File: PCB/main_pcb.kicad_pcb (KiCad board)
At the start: 2 copper layers, 116.9 x 116.9 mm, 39 parts, among them P1 SEN, P2 SRV, P3 PWR, P4 LED, P5 M1, P6 M2, P7 CONN_02X03, P8 CONN_02X03, Q1 5LN01SP, U1 Teensy_3.1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

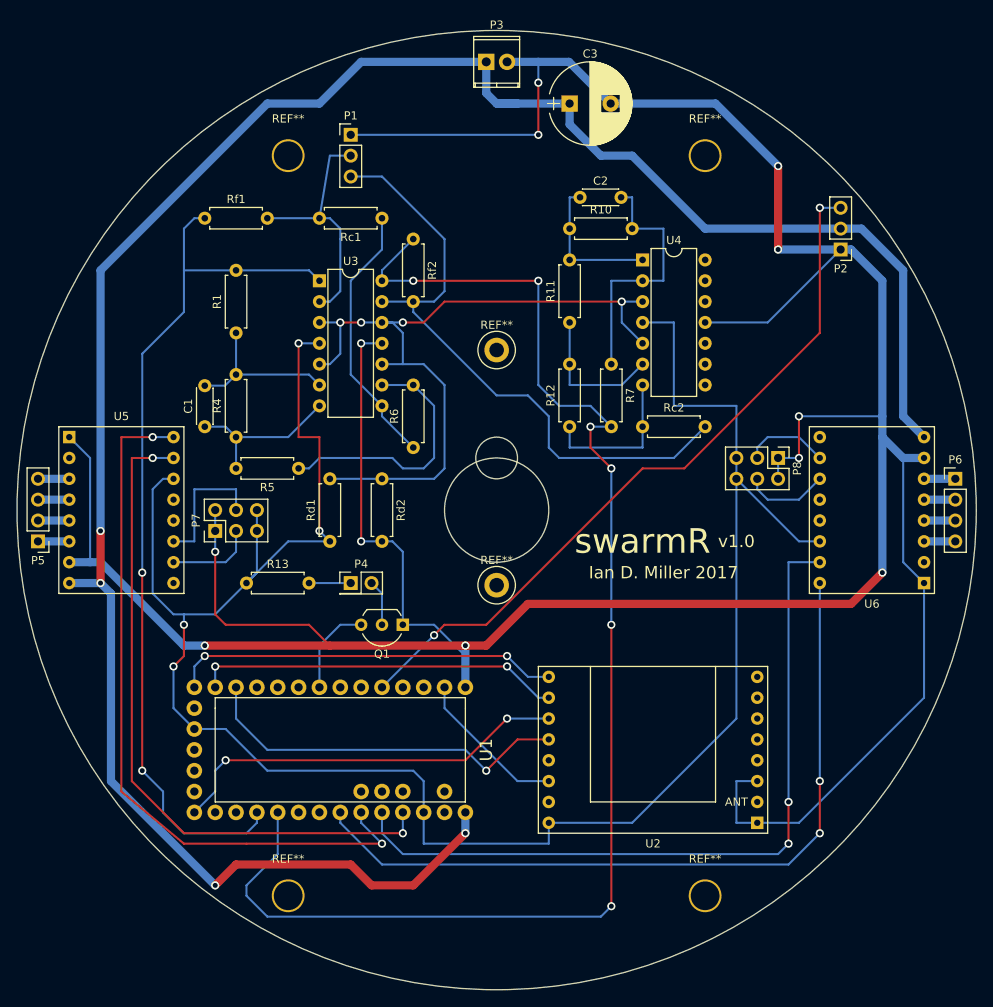
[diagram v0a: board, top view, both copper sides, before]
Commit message: Updated pcb layout for easier fabrication
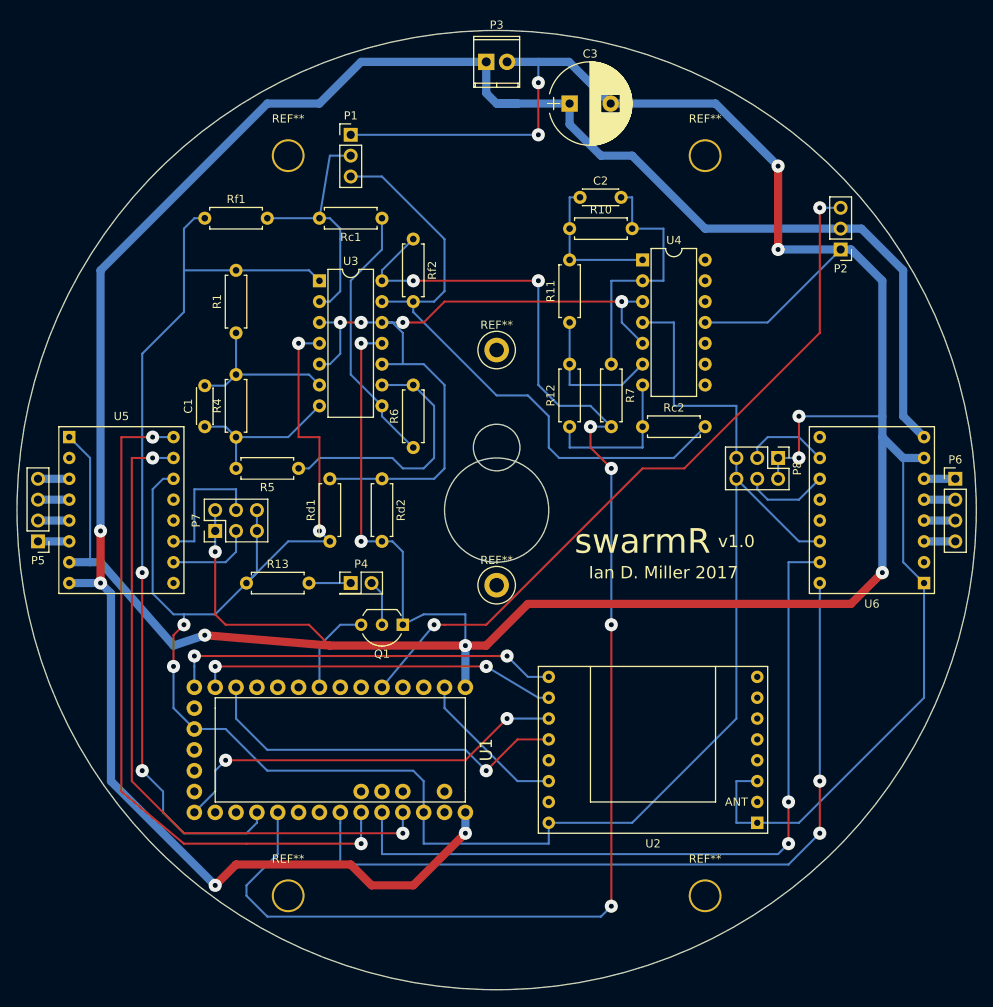
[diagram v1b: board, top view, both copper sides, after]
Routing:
- net GND: track 454.5 -> 458.9 mm
- net /DIR1: track 88.4 -> 84.8 mm
- net /DIR2: track 93.9 -> 96.8 mm
- net /STEP2: track 91.7 -> 93.2 mm
- net /MISO: track 47.3 -> 48.0 mm
- net /MOSI: track 44.8 -> 44.2 mm
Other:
- outline, holes or cut-outs redrawn
- net class Default: via_dia 1 -> 1.6

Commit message: minor pcb and BOM adjustments
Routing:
- net /RadCS: vias 1 -> 2

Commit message: Small pcb adjustments
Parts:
- R13: value R -> 10R
- Rc1, Rc2: value 15k -> 240k
- Rf1, Rf2: value 51k -> 750k
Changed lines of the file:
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@@
     (links 99)
     (no_connects 0)
-    (area 79.921196 35.01412 215.01 165.260001)
+    (area 79.921196 36.741196 196.938804 153.758804)
     (thickness 1.6)
     (drawings 9)
@@
       (padsonsilk false)
       (subtractmaskfromsilk false)
-      (outputformat 1)
+      (outputformat 4)
       (mirror false)
       (drillshape 0)
@@
       (effects (font (size 1 1) (thickness 0.15)))
     )
-    (fp_text value R (at 3.81 2.31) (layer F.Fab)
+    (fp_text value 10R (at 3.81 2.31) (layer F.Fab)
       (effects (font (size 1 1) (thickness 0.15)))
     )
@@
       (effects (font (size 1 1) (thickness 0.15)))
     )
-    (fp_text value 15k (at 3.81 2.31 180) (layer F.Fab)
+    (fp_text value 240k (at 3.81 2.31 180) (layer F.Fab)
       (effects (font (size 1 1) (thickness 0.15)))
     )
@@
       (effects (font (size 1 1) (thickness 0.15)))
     )
-    (fp_text value 15k (at 3.81 2.31) (layer F.Fab)
+    (fp_text value 240k (at 3.81 2.31) (layer F.Fab)
       (effects (font (size 1 1) (thickness 0.15)))
     )
@@
       (effects (font (size 1 1) (thickness 0.15)))
     )
-    (fp_text value 51k (at 3.81 2.31) (layer F.Fab)
+    (fp_text value 750k (at 3.81 2.31) (layer F.Fab)
       (effects (font (size 1 1) (thickness 0.15)))
     )
@@
       (effects (font (size 1 1) (thickness 0.15)))
     )
-    (fp_text value 51k (at 3.81 2.31 270) (layer F.Fab)
+    (fp_text value 750k (at 3.81 2.31 270) (layer F.Fab)
       (effects (font (size 1 1) (thickness 0.15)))
     )
@@
   (segment (start 140.97 128.27) (end 132.08 119.38) (width 0.25) (layer B.Cu) (net 37))
   (via (at 140.97 123.19) (size 1.6) (drill 0.6) (layers F.Cu B.Cu) (net 45))
-  (segment (start 140.97 123.19) (end 144.78 123.19) (width 0.25) (layer B.Cu) (net 45) (status 800000))
+  (segment (start 140.97 123.19) (end 144.78 123.19) (width 0.25) (layer B.Cu) (net 45))
   (segment (start 106.68 116.84) (end 106.68 120.65) (width 0.25) (layer B.Cu) (net 45))
   (segment (start 137.16 127) (end 140.97 123.19) (width 0.25) (layer F.Cu) (net 45))

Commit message: PCB revisions
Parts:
- added P9: Range, Pin_Headers:Pin_Header_Straight_2x01_Pitch2.54mm, F.Cu at (121.9, 47.0)
- moved P2 105.1 mm to (86.4, 110.5), turned to 0 degrees
- moved R13 53.0 mm to (144.8, 142.2), turned to 180 degrees
- moved P4 36.9 mm to (118.1, 141.0), turned to 270 degrees
- moved Q1 36.8 mm to (127.0, 146.1), turned to 90 degrees
- moved U1 32.9 mm to (102.9, 132.1), turned to 0 degrees
- moved P3 2.54 mm to (139.7, 40.6), turned to 180 degrees
- moved P1 1.27 mm to (121.9, 49.5)
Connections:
- P3 pad 1: VDD -> GND
- P3 pad 2: GND -> VDD
- Q1 pad 2: Net-(P4-Pad2) -> Net-(P4-Pad1)
- R13 pad 2: Net-(P4-Pad1) -> Net-(P4-Pad2)
- U1 pad 1: Net-(U1-Pad1) -> /Reset
- U2 pad 15: Net-(U2-Pad15) -> /RadInt
- U2 pad 5: Net-(U2-Pad5) -> /Reset
- U2 pad 6: /RadInt -> Net-(U2-Pad6)
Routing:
- net Net-(P9-Pad1): track 0.00 -> 95.6 mm, vias 0 -> 6
- net Net-(P9-Pad2): track 0.00 -> 85.1 mm, vias 0 -> 2
- net GND: track 458.9 -> 531.2 mm, vias 12 -> 15
- net /RadInt: track 18.9 -> 82.2 mm
- net /AnalogFilter2/Out: track 169.2 -> 107.8 mm, vias 6 -> 4
- net /Reset: track 0.00 -> 57.7 mm, vias 0 -> 2
- net VDD: track 268.7 -> 213.1 mm, vias 4 -> 2
- net /SRV: track 89.4 -> 33.9 mm, vias 2 -> 0
- net /STEP1: track 82.6 -> 44.8 mm, vias 2 -> 4
- net /SCK: track 49.4 -> 13.0 mm, vias 2 -> 0
- net /AnalogFilter1/Out: track 108.7 -> 82.3 mm
- net /DIR2: track 96.8 -> 73.6 mm
- net /MISO: track 48.0 -> 25.7 mm
- net Net-(P4-Pad2): track 5.61 -> 25.3 mm
- net /RadCS: track 46.1 -> 31.8 mm
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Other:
- net class Default: trace_width 0.25 -> 0.35
- board text added: "v1.1"
- board text removed: "v1.0"

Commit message: Recalibrated resistor gains
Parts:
- Rc1, Rc2: value 240k -> 36k
- Rf1, Rf2: value 750k -> 68k
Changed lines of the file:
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@@
       (effects (font (size 1 1) (thickness 0.15)))
     )
-    (fp_text value 240k (at 3.81 2.31 180) (layer F.Fab)
+    (fp_text value 36k (at 3.81 2.31 180) (layer F.Fab)
       (effects (font (size 1 1) (thickness 0.15)))
     )
@@
       (effects (font (size 1 1) (thickness 0.15)))
     )
-    (fp_text value 240k (at 3.81 2.31) (layer F.Fab)
+    (fp_text value 36k (at 3.81 2.31) (layer F.Fab)
       (effects (font (size 1 1) (thickness 0.15)))
     )
@@
       (effects (font (size 1 1) (thickness 0.15)))
     )
-    (fp_text value 750k (at 3.81 2.31) (layer F.Fab)
+    (fp_text value 68k (at 3.81 2.31) (layer F.Fab)
       (effects (font (size 1 1) (thickness 0.15)))
     )
@@
       (effects (font (size 1 1) (thickness 0.15)))
     )
-    (fp_text value 750k (at 3.81 2.31 270) (layer F.Fab)
+    (fp_text value 68k (at 3.81 2.31 270) (layer F.Fab)
       (effects (font (size 1 1) (thickness 0.15)))
     )
